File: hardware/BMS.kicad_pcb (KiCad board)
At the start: 2 copper layers, 100 x 100 mm, 15 parts, among them J1 RJ45, J2 TESLA_BMS, J5 POWER, J7 CURRENT_SENSOR, U2 CAN BUS, U3 RELAY_MODULE, U4 MCP3421, U5 L7805, U6 STEP_UP, U7 ESP32-DEVKIT-V1

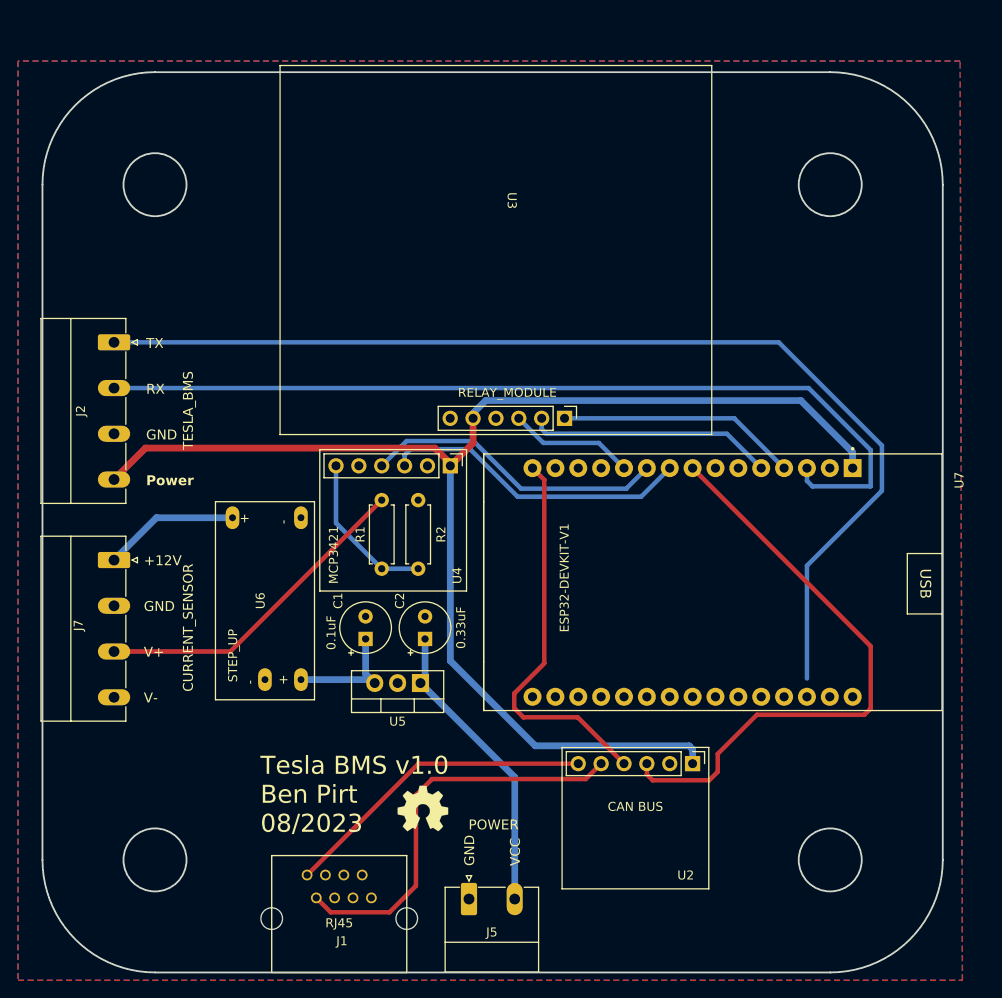
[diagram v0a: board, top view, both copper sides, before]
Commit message: Update PCB to support WT32-ETH01 module (v1.1)
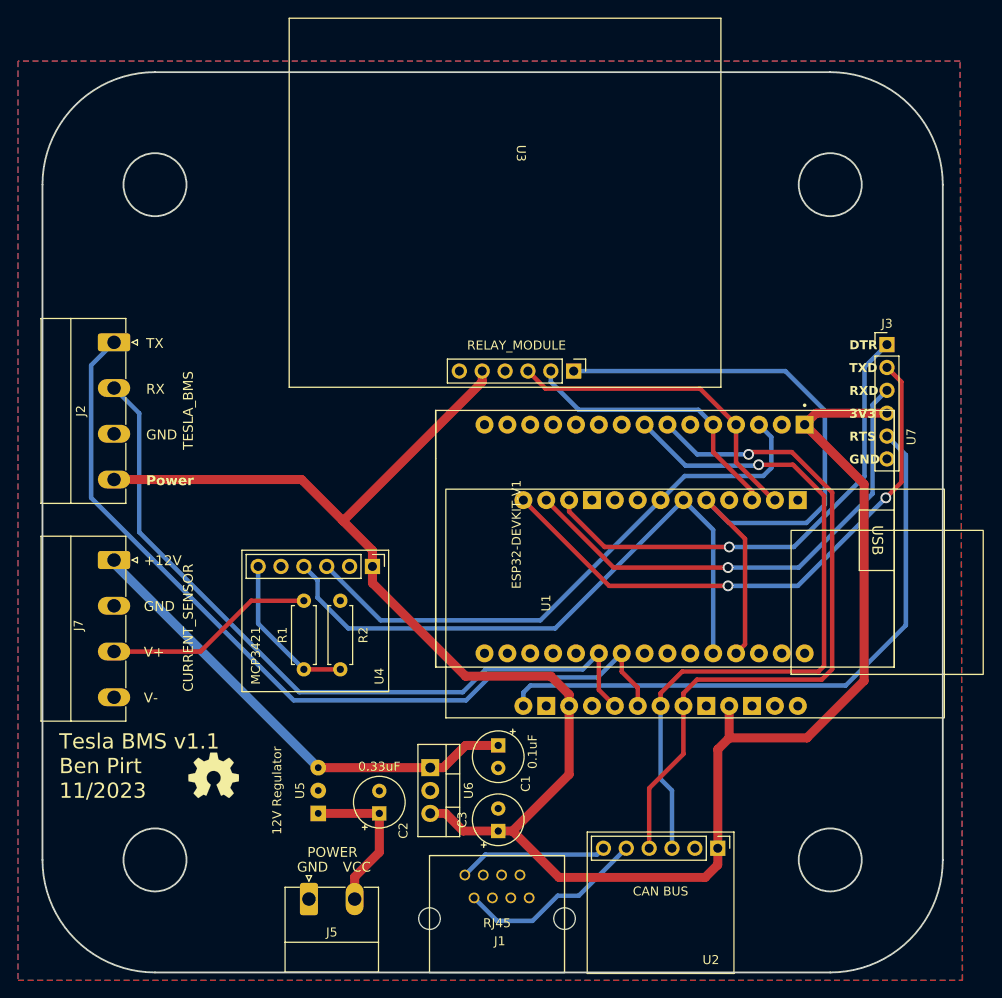
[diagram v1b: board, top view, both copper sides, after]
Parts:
- added C3: 0.1uF, Capacitor_THT:CP_Radial_Tantal_D5.5mm_P2.50mm, F.Cu at (150.6, 134.3)
- added J3: Conn_01x06_Pin, Connector_PinHeader_2.54mm:PinHeader_1x06_P2.54mm_Vertical, F.Cu at (193.8, 80.3)
- added U1: WT32_ETH01, BMSLibrary:WT32_ETH01, F.Cu at (149.6, 108.3)
- U5: value L7805 -> 12V Regulator; footprint Package_TO_SOT_THT:TO-220-3_Vertical -> BMSLibrary:12V_REGULATOR
- U6: value STEP_UP -> L7833; footprint BMSLibrary:STEP_UP_MODULE -> Package_TO_SOT_THT:TO-220-3_Vertical
- moved U6 26.1 mm to (143.1, 127.3), turned to -90 degrees
- moved G*** 23.5 mm to (119.0, 128.1)
- moved C2 20.0 mm to (137.4, 132.3)
- moved C1 18.9 mm to (150.6, 124.8), turned to -90 degrees
- moved J5 17.8 mm to (129.6, 141.8)
- moved J1 17.5 mm to (150.5, 144.0)
- moved U5 16.5 mm to (130.6, 129.8), turned to 90 degrees
- moved U4 14.1 mm to (130.3, 113.7)
- moved R2 14.1 mm to (133.1, 116.3)
- moved R1 14.1 mm to (129.0, 116.3)
- moved U2 9.80 mm to (168.7, 145.0)
- moved U7 7.19 mm to (169.1, 101.9)
- moved U3 5.35 mm to (152.7, 59.0)
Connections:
- C1 pad 1: +5V -> +12V
- J2 pad 1: /can-tx -> /bms-tx
- U5 pad 3: +5V -> +12V
- U6 pad 1: GND -> +12V
- U6 pad 2: +5V -> GND
- U6 pad 3: GND -> +3.3V
- U7 pad 10: /SDA -> unconnected-(U7-D19-Pad10)
- U7 pad 11: /RELAY3 -> unconnected-(U7-D21-Pad11)
- U7 pad 15: /can-rx -> unconnected-(U7-D23-Pad15)
- U7 pad 21: unconnected-(U7-D32-Pad21) -> /bms-rx
- U7 pad 22: unconnected-(U7-D33-Pad22) -> /bms-tx
- U7 pad 26: unconnected-(U7-D14-Pad26) -> /SDA
- U7 pad 27: unconnected-(U7-D12-Pad27) -> /RELAY1
- U7 pad 28: /bms-tx -> unconnected-(U7-D13-Pad28)
- U7 pad 3: /bms-rx -> /SCL
- U7 pad 30: +5V -> unconnected-(U7-VIN-Pad30)
- U7 pad 4: /RELAY1 -> /RELAY3
- U7 pad 7: unconnected-(U7-TX2-Pad7) -> /can-rx
- U7 pad 9: /SCL -> unconnected-(U7-D18-Pad9)
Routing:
- net /can-tx: track 185.1 -> 79.4 mm, vias 0 -> 1
- net /bms-tx: track 0.00 -> 95.3 mm
- net /RTS: track 0.00 -> 68.9 mm
- net +3.3V: track 147.8 -> 215.5 mm
- net /TXD: track 0.00 -> 64.1 mm, vias 0 -> 2
- net /RXD: track 0.00 -> 54.9 mm, vias 0 -> 1
- net /DTR: track 0.00 -> 54.6 mm, vias 0 -> 1
- net /RELAY1: track 26.7 -> 74.4 mm
- net +12V: track 15.1 -> 53.5 mm
- net /SDA: track 33.7 -> 70.4 mm
- net /can-rx: track 43.3 -> 77.7 mm, vias 0 -> 1
- net /SCL: track 34.4 -> 64.2 mm
- net Net-(U2-CANH): track 45.0 -> 21.3 mm
- net /RELAY3: track 14.0 -> 35.8 mm
- net Net-(U2-CANL): track 35.2 -> 16.6 mm
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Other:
- board text added: "3V3"
- board text added: "DTR"
- board text added: "RTS"
- board text added: "RXD"
- board text added: "TXD"
- board text added: "Tesla BMS v1.1 Ben Pirt 11/2023"
- board text removed: "Tesla BMS v1.0 Ben Pirt 08/2023"

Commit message: Fix some hardware issues - increment to v1.3
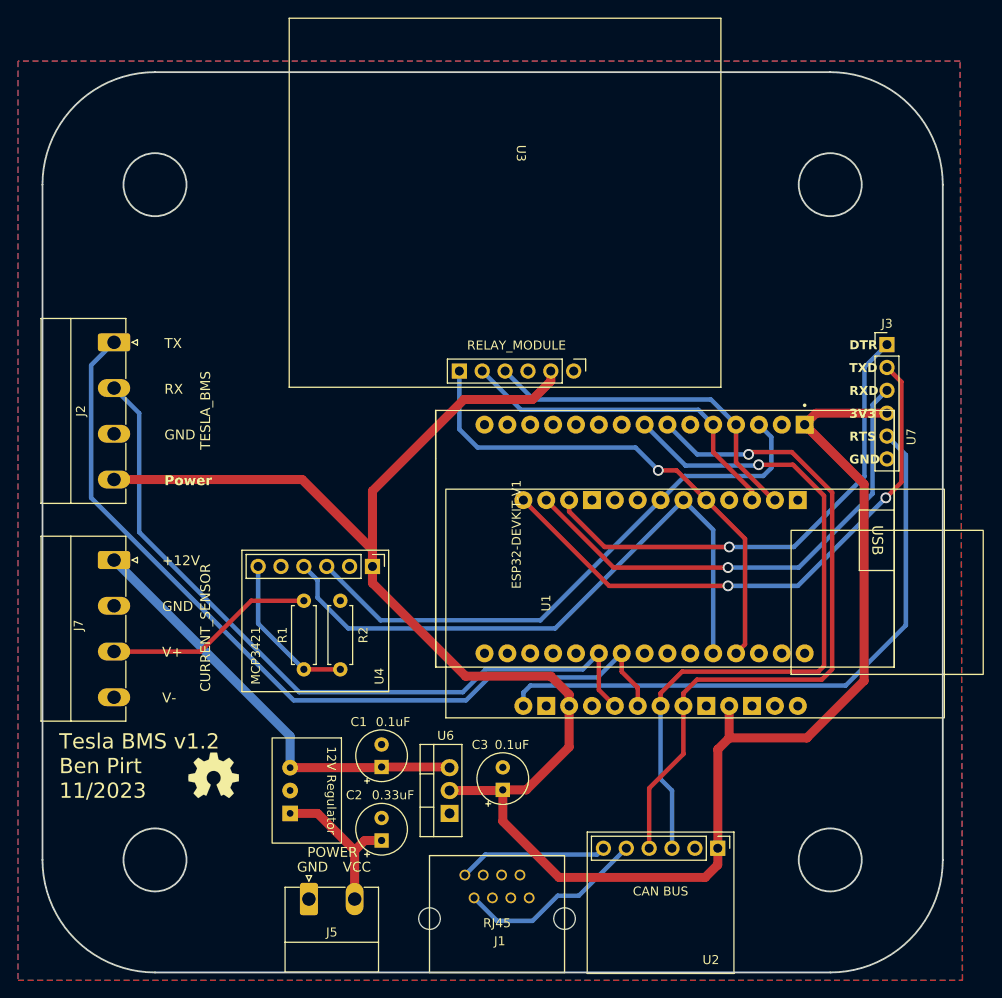
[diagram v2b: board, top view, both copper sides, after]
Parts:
- moved C1 13.2 mm to (137.7, 127.2), turned to 90 degrees
- moved U6 5.51 mm to (145.2, 132.3), turned to 90 degrees
- moved C3 4.60 mm to (151.1, 129.7)
- moved U5 3.12 mm to (127.5, 129.8), turned to -90 degrees
- moved C2 3.02 mm to (137.7, 135.3)
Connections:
- U6 pad 1: +12V -> GND
- U6 pad 2: GND -> +3.3V
- U6 pad 3: +3.3V -> +12V
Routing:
- net /RELAY1: track 74.4 -> 56.4 mm, vias 0 -> 1
- net +3.3V: track 215.5 -> 225.3 mm
- net /RELAY2: track 31.4 -> 38.3 mm
- net +12V: track 53.5 -> 48.9 mm
- net /RELAY3: track 35.8 -> 38.4 mm
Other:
- board text added: "Tesla BMS v1.2 Ben Pirt 11/2023"
- board text removed: "Tesla BMS v1.1 Ben Pirt 11/2023"
